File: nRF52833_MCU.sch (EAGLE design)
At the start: 45 parts, among them IC1 SKY13415-485LF, J100 DEBUG_CONNECTOR, J3 282834-2, U1 nRF52833-QIAA, X1 32MHz, X2 32.768kHz, X3 22-23-2031

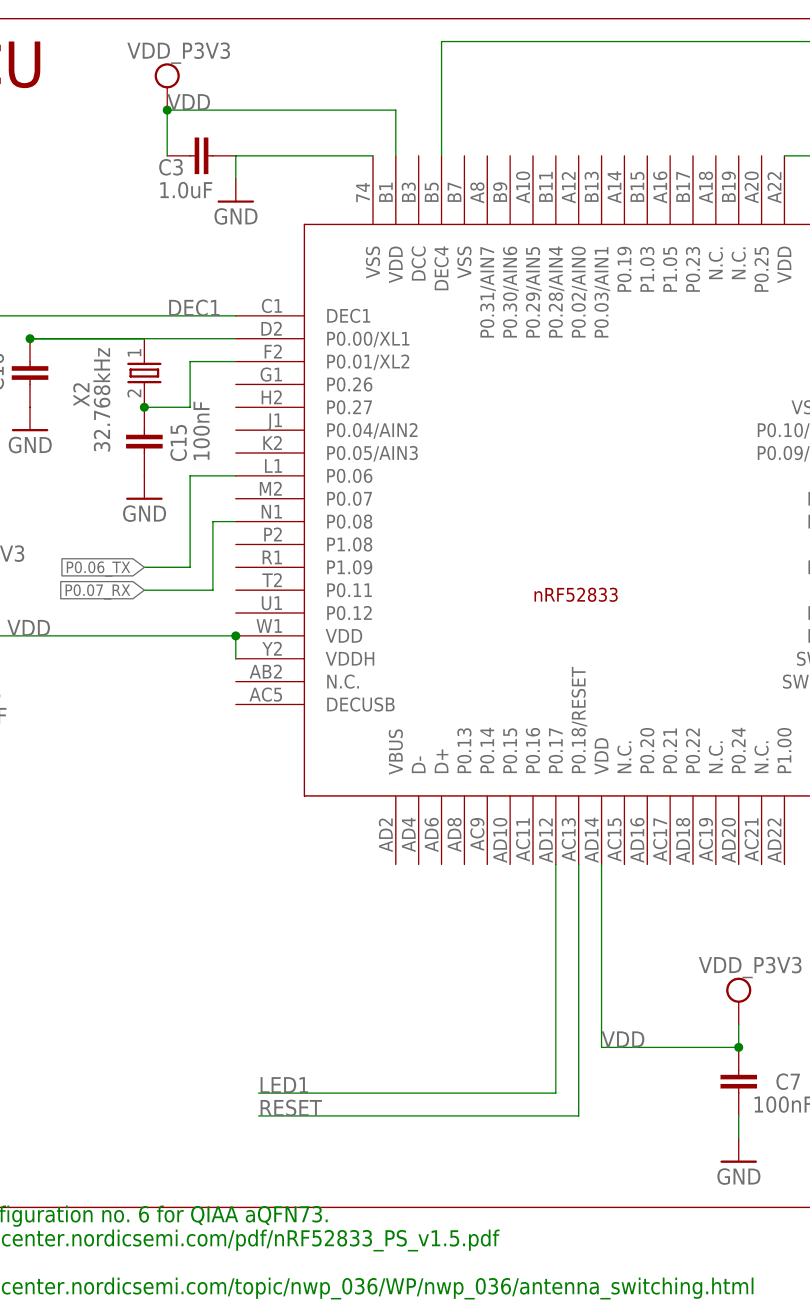
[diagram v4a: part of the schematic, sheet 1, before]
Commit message: Disconnect reset
Signed-off-by: Florian Depraz <florian.depraz@outlook.com>
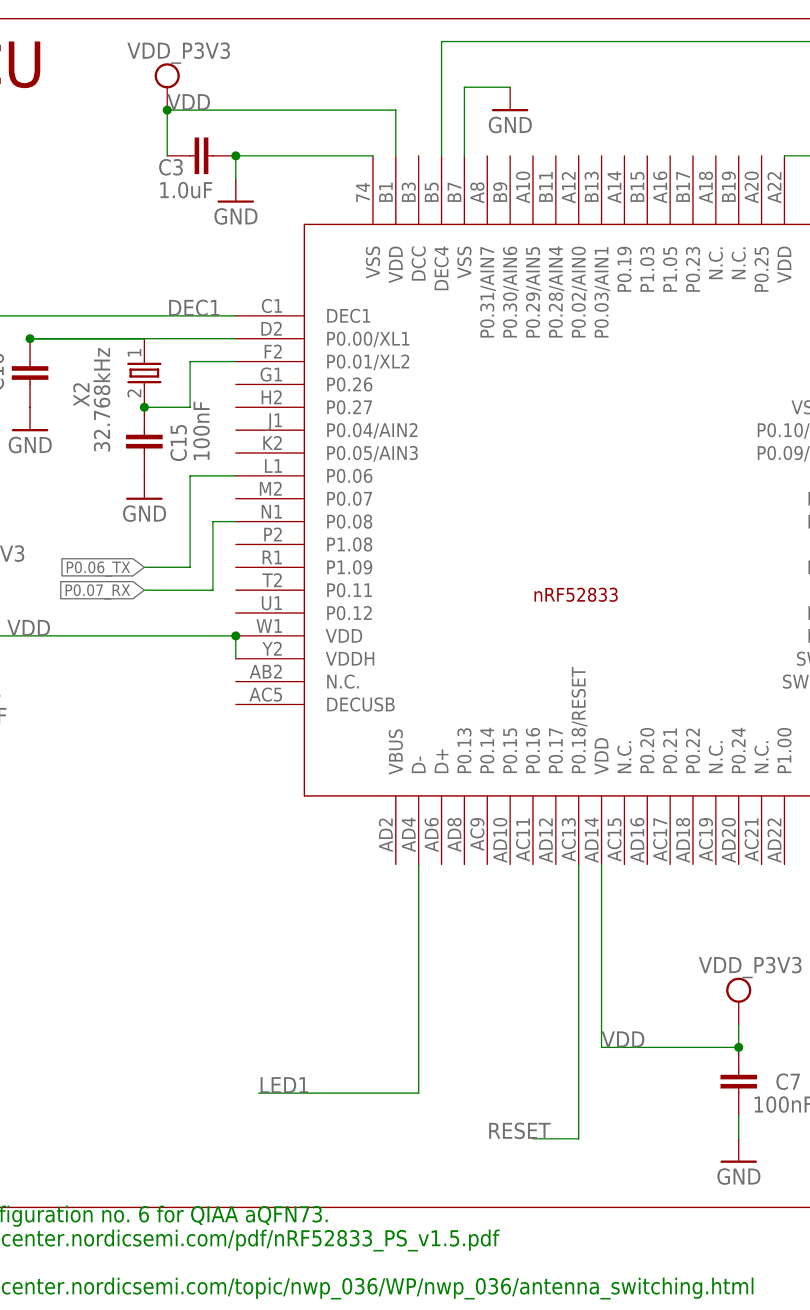
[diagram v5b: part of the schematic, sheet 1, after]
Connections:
- net GND: now also U1.VSS@2
- net LED1: now also U1.D-; no longer U1.P0.17
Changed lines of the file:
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@@
 <part name="ANT4" library="2450AT18B100E" deviceset="2450AT18B100E" device=""/>
 <part name="ANT5" library="2450AT18B100E" deviceset="2450AT18B100E" device=""/>
+<part name="GND18" library="supply1" deviceset="GND" device=""/>
 </parts>
 <sheets>
@@
 <attribute name="VALUE" x="167.64" y="109.22" size="1.778" layer="96" rot="MR0"/>
 </instance>
+<instance part="GND18" gate="1" x="73.66" y="165.1" smashed="yes" rot="MR0">
+<attribute name="VALUE" x="76.2" y="162.56" size="1.778" layer="96" rot="MR0"/>
+</instance>
 </instances>
 <busses>
@@
 </segment>
 <segment>
-<pinref part="U1" gate="A" pin="P0.17"/>
-<wire x1="45.72" y1="55.88" x2="78.74" y2="55.88" width="0.1524" layer="91"/>
-<wire x1="78.74" y1="55.88" x2="78.74" y2="81.28" width="0.1524" layer="91"/>
+<wire x1="45.72" y1="55.88" x2="63.5" y2="55.88" width="0.1524" layer="91"/>
 <label x="45.72" y="55.88" size="1.778" layer="95"/>
+<pinref part="U1" gate="A" pin="D-"/>
+<wire x1="63.5" y1="81.28" x2="63.5" y2="55.88" width="0.1524" layer="91"/>
 </segment>
 </net>
@@
 <net name="RESET" class="0">
 <segment>
-<pinref part="U1" gate="A" pin="P0.18/RESET"/>
-<label x="45.72" y="53.34" size="1.778" layer="95"/>
-<wire x1="45.72" y1="53.34" x2="81.28" y2="53.34" width="0.1524" layer="91"/>
-<wire x1="81.28" y1="53.34" x2="81.28" y2="81.28" width="0.1524" layer="91"/>
-</segment>
-<segment>
 <pinref part="J100" gate="G$1" pin="10"/>
 <wire x1="139.7" y1="55.88" x2="124.46" y2="55.88" width="0.1524" layer="91"/>
 <label x="124.46" y="55.88" size="1.778" layer="95"/>
+</segment>
+<segment>
+<pinref part="U1" gate="A" pin="P0.18/RESET"/>
+<wire x1="81.28" y1="81.28" x2="81.28" y2="50.8" width="0.1524" layer="91"/>
+<wire x1="81.28" y1="50.8" x2="76.2" y2="50.8" width="0.1524" layer="91"/>
+<label x="71.12" y="50.8" size="1.778" layer="95"/>
 </segment>
 </net>
@@
 </segment>
 </net>
-<net name="GND" class="1">
+<net name="GND" class="0">
 <segment>
 <pinref part="C6" gate="C$1" pin="2"/>
@@
 <pinref part="GND17" gate="1" pin="GND"/>
 <pinref part="C15" gate="C$1" pin="1"/>
-</segment>
-<segment>
-<pinref part="C3" gate="C$1" pin="2"/>
-<wire x1="43.18" y1="157.48" x2="43.18" y2="160.02" width="0.1524" layer="91"/>
-<pinref part="U1" gate="A" pin="VSS@1"/>
-<wire x1="43.18" y1="160.02" x2="58.42" y2="160.02" width="0.1524" layer="91"/>
-<pinref part="GND2" gate="1" pin="GND"/>
 </segment>
 <segment>
@@
 <wire x1="165.1" y1="114.3" x2="172.72" y2="114.3" width="0.1524" layer="91"/>
 <junction x="165.1" y="114.3"/>
+</segment>
+<segment>
+<pinref part="C3" gate="C$1" pin="2"/>
+<pinref part="GND2" gate="1" pin="GND"/>
+<wire x1="43.18" y1="160.02" x2="43.18" y2="157.48" width="0.1524" layer="91"/>
+<pinref part="U1" gate="A" pin="VSS@1"/>
+<wire x1="43.18" y1="160.02" x2="58.42" y2="160.02" width="0.1524" layer="91"/>
+<junction x="43.18" y="160.02"/>
+</segment>
+<segment>
+<pinref part="U1" gate="A" pin="VSS@2"/>
+<wire x1="68.58" y1="160.02" x2="68.58" y2="167.64" width="0.1524" layer="91"/>
+<wire x1="68.58" y1="167.64" x2="73.66" y2="167.64" width="0.1524" layer="91"/>
+<pinref part="GND18" gate="1" pin="GND"/>
 </segment>
 </net>
@@
 </segment>
 </net>
-<net name="GND" class="1">
+<net name="GND" class="0">
 <segment>
 <pinref part="GND24" gate="1" pin="GND"/>

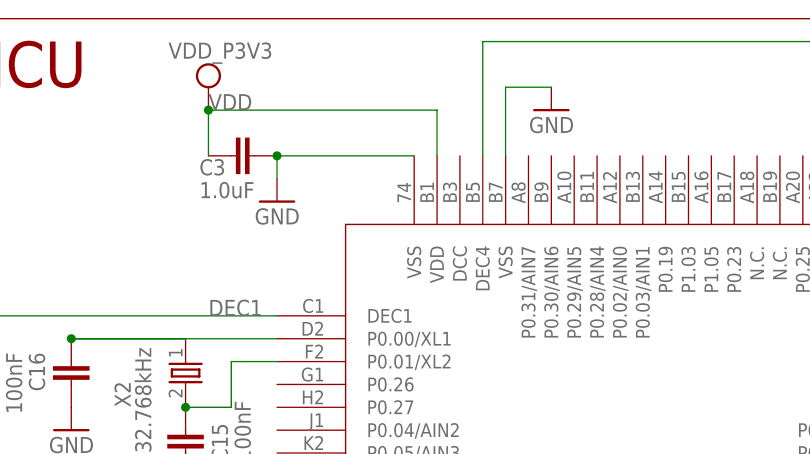
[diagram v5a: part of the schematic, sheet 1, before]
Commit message: Reduce signal size
Signed-off-by: Florian Depraz <florian.depraz@outlook.com>
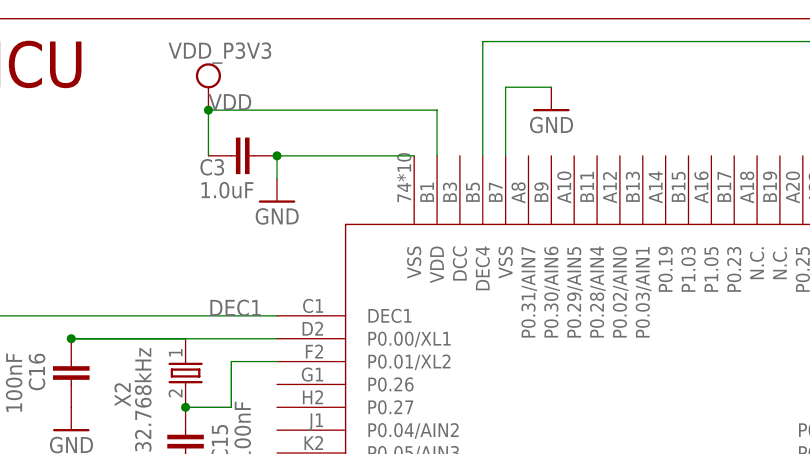
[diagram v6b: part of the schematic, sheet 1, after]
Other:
- moved on the sheet: U1

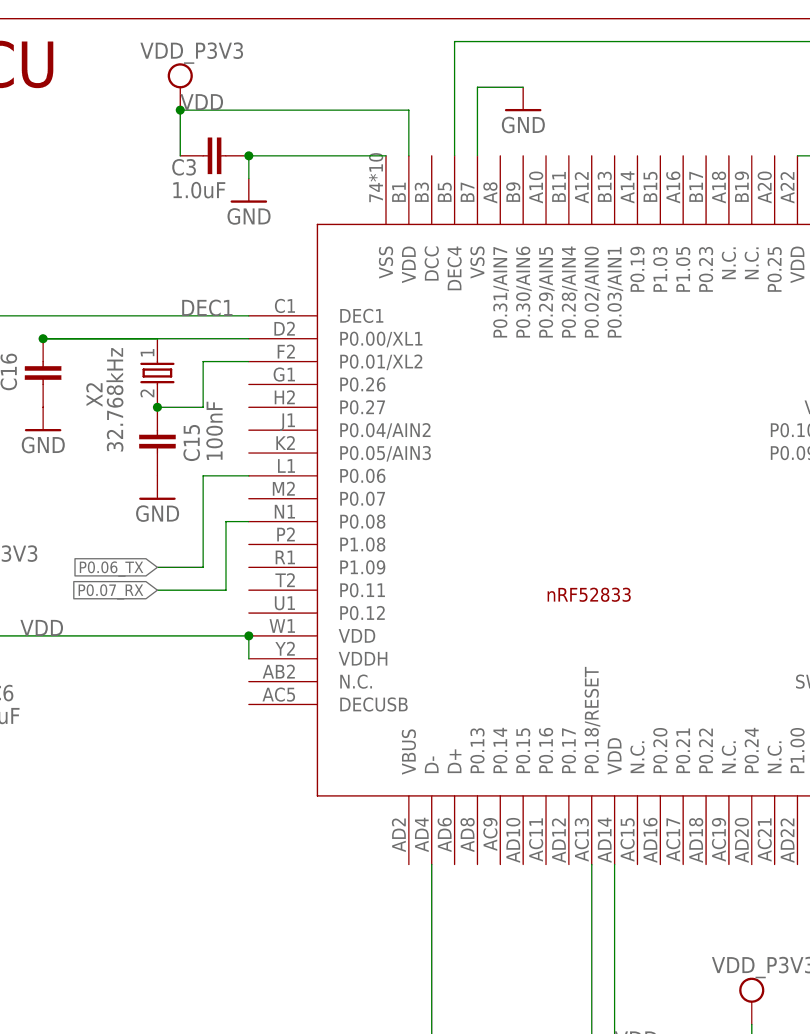
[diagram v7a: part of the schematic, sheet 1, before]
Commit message: Make sure to respect the design rules
Signed-off-by: Florian Depraz <florian.depraz@outlook.com>
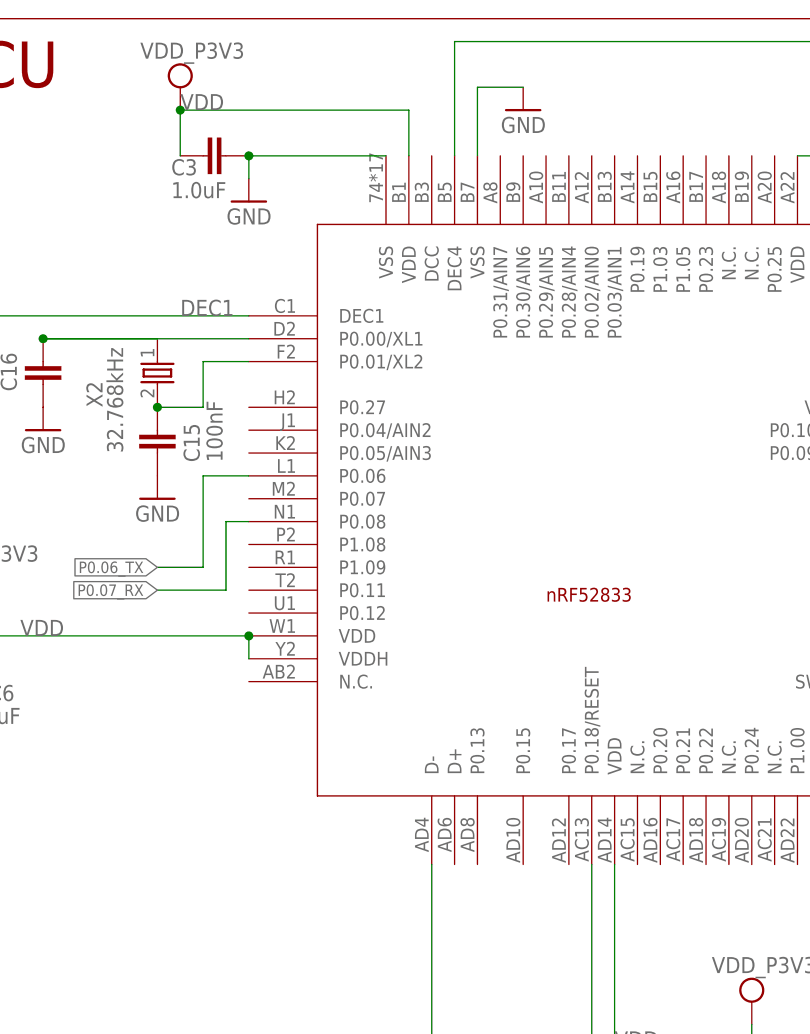
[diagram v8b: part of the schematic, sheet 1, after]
